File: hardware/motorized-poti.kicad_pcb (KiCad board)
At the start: 2 copper layers, 100 x 20 mm, 31 parts, among them J1 AKL_5_2, P1 CON-SENSOR2, P2 MOTORIZED_POTI, P3 BOOT, P4 CONN_02X04, P5 CONN_02X04, U1 XMC1XXX24, U2 ZXBM5210, U3 DRILL, U4 DRILL, U5 DRILL, U6 DRILL

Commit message: Fix logos
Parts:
- G***: moved to B.Cu
- moved G*** 70.5 mm to (99.3, 100.6)
- moved VAL 1.10 mm to (107.5, 100.6)
- moved G*** 0.90 mm to (115.5, 100.6)

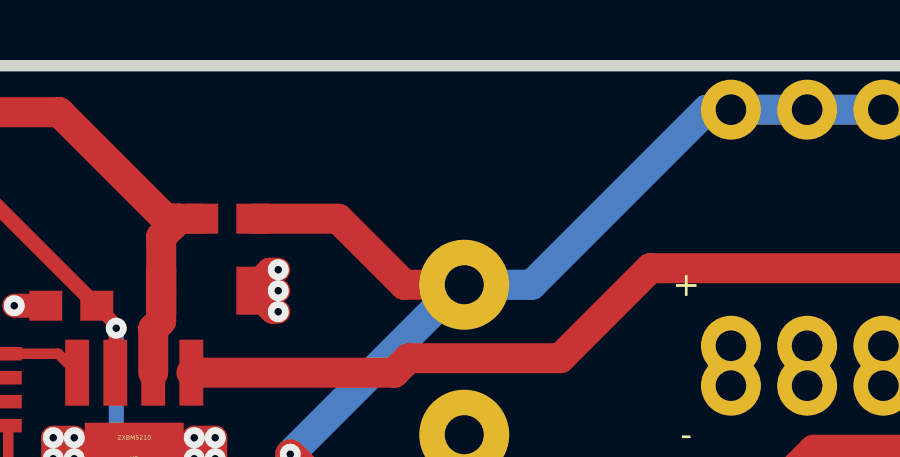
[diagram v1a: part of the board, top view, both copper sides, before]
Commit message: connector distance to short hintt
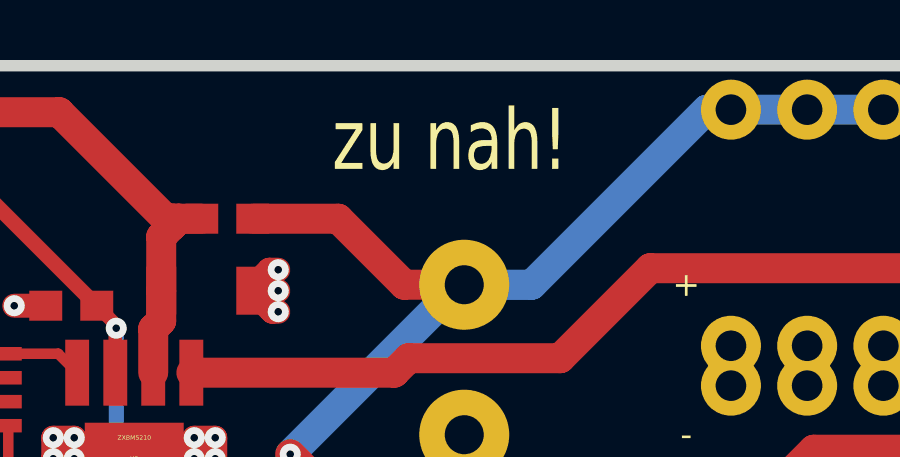
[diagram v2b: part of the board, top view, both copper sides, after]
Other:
- board text added: "zu nah!"
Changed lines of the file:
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@@
-(kicad_pcb (version 4) (host pcbnew 4.0.2+dfsg1-stable)
+(kicad_pcb (version 4) (host pcbnew 4.0.6-e0-6349~53~ubuntu16.04.1)
   (general
     (links 70)
     (no_connects 0)
-    (area 77.409499 90.459499 177.790501 110.840501)
+    (area 70.875139 90.459499 282.795857 162.890793)
     (thickness 1.6002)
-    (drawings 13)
+    (drawings 14)
     (tracks 235)
     (zones 0)
@@
       (net 5 "Net-(P2-PadB)"))
   )
+  (gr_text "zu nah!" (at 141.425 93.15) (layer F.SilkS)
+    (effects (font (size 2.032 1.524) (thickness 0.3048)))
+  )
   (gr_line (start 77.6 93.15) (end 77.6 108.15) (angle 90) (layer Edge.Cuts) (width 0.381))

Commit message: specify part values
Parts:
- C3: value TBD -> 47uF/10V
- L1: value INDUCT -> DNP
- L2: value INDUCT -> FB
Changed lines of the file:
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@@
     (links 70)
     (no_connects 0)
-    (area 70.875139 90.459499 282.795857 162.890793)
+    (area 77.409499 90.459499 177.790501 110.840501)
     (thickness 1.6002)
     (drawings 14)
@@
       (effects (font (size 0.3 0.3) (thickness 0.075)))
     )
-    (fp_text value TBD (at 0 -0.65 180) (layer F.Fab)
+    (fp_text value 47uF/10V (at 0 -0.65 180) (layer F.Fab)
       (effects (font (size 0.3 0.3) (thickness 0.075)))
     )
@@
       (effects (font (size 0.2 0.2) (thickness 0.05)))
     )
-    (fp_text value INDUCT (at 0.05 -0.375 90) (layer F.Fab)
+    (fp_text value DNP (at 0.05 -0.375 90) (layer F.Fab)
       (effects (font (size 0.2 0.2) (thickness 0.05)))
     )
@@
       (effects (font (size 0.2 0.2) (thickness 0.05)))
     )
-    (fp_text value INDUCT (at 0.05 -0.375 180) (layer F.Fab)
+    (fp_text value FB (at 0.05 -0.375 180) (layer F.Fab)
       (effects (font (size 0.2 0.2) (thickness 0.05)))
     )

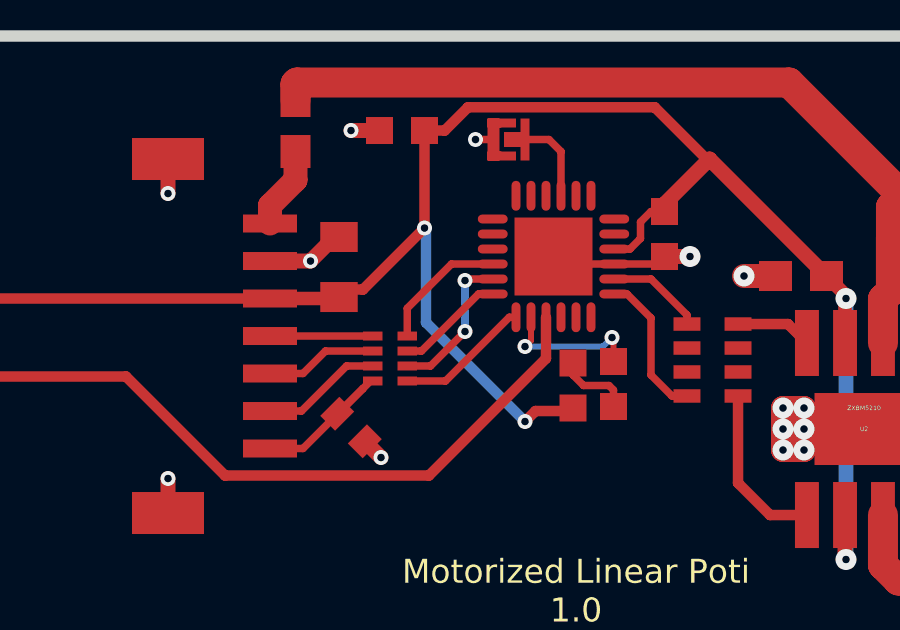
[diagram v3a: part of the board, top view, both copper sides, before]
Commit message: Fix SPI pins
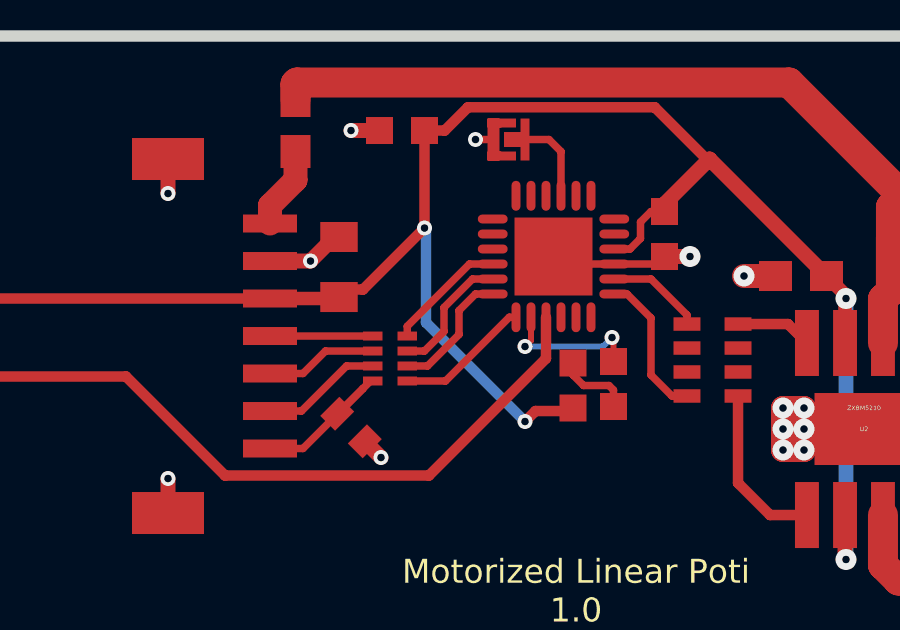
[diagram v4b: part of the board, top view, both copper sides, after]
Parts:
- C2: footprint kicad-libraries:C0805 -> C0805
- C4, C5: footprint kicad-libraries:C0603F -> C0603F
- C6: footprint kicad-libraries:C0402E -> C0402E
- D1: footprint kicad-libraries:D0603F -> D0603F
- J1: footprint kicad-libraries:AKL_5_2 -> AKL_5_2
- L1, L2: footprint kicad-libraries:C0603E -> C0603E
- P1: footprint kicad-libraries:CON-SENSOR2 -> CON-SENSOR2
- P2: footprint kicad-libraries:MOTORIZED_POTI -> MOTORIZED_POTI
- R1: footprint kicad-libraries:R0603F -> R0603F
- RP1: footprint kicad-libraries:4X0603 -> 4X0603
- RP3: footprint kicad-libraries:4X0402 -> 4X0402
- U2: footprint kicad-libraries:SO-8-EP -> SO-8-EP
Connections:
- P2 pad 2: (no net) -> Net-(P2-Pad2)
- RP1 pad 2: (no net) -> Net-(RP1-Pad2)
- RP1 pad 3: (no net) -> Net-(RP1-Pad3)
- RP1 pad 6: (no net) -> Net-(RP1-Pad6)
- RP1 pad 7: (no net) -> Net-(RP1-Pad7)
- U1 pad 11: (no net) -> Net-(U1-Pad11)
- U1 pad 12: (no net) -> Net-(U1-Pad12)
- U1 pad 13: (no net) -> Net-(U1-Pad13)
- U1 pad 14: (no net) -> Net-(U1-Pad14)
- U1 pad 16: (no net) -> Net-(U1-Pad16)
- U1 pad 17: (no net) -> Net-(U1-Pad17)
- U1 pad 18: (no net) -> Net-(U1-Pad18)
- U1 pad 19: (no net) -> Net-(U1-Pad19)
- U1 pad 20: (no net) -> Net-(U1-Pad20)
- U1 pad 21: (no net) -> Net-(U1-Pad21)
- U1 pad 23: S-MOSI -> S-CLK
- U1 pad 24: S-CLK -> S-MOSI
- U1 pad 4: (no net) -> Net-(U1-Pad4)
- U1 pad 5: (no net) -> Net-(U1-Pad5)
- U1 pad 6: (no net) -> Net-(U1-Pad6)
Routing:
- net S-MOSI: track 5.05 -> 4.31 mm, vias 2 -> 0
- net S-CLK: track 3.64 -> 4.31 mm

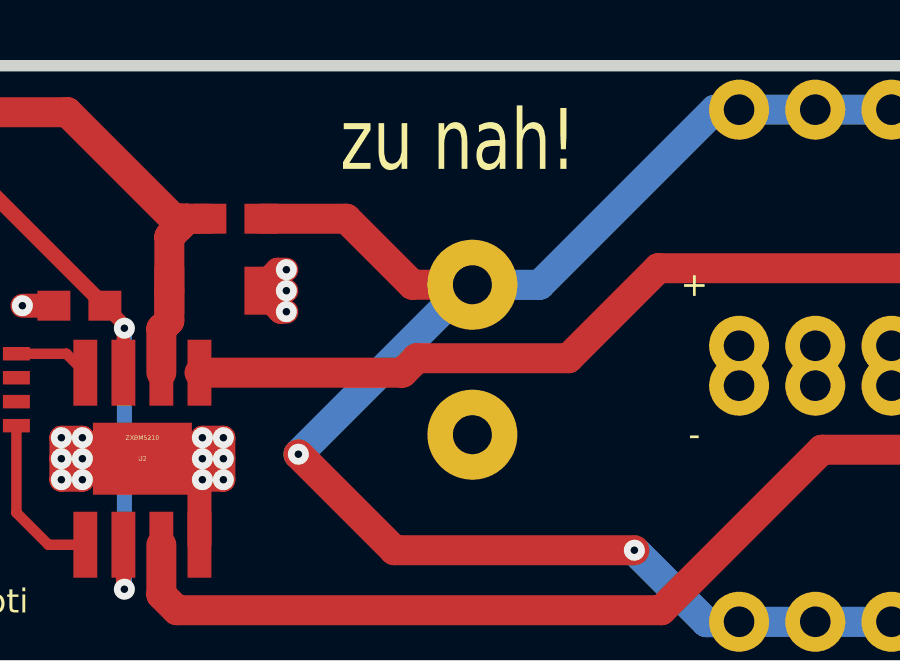
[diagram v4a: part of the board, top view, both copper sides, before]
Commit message: Fix orientation of J1
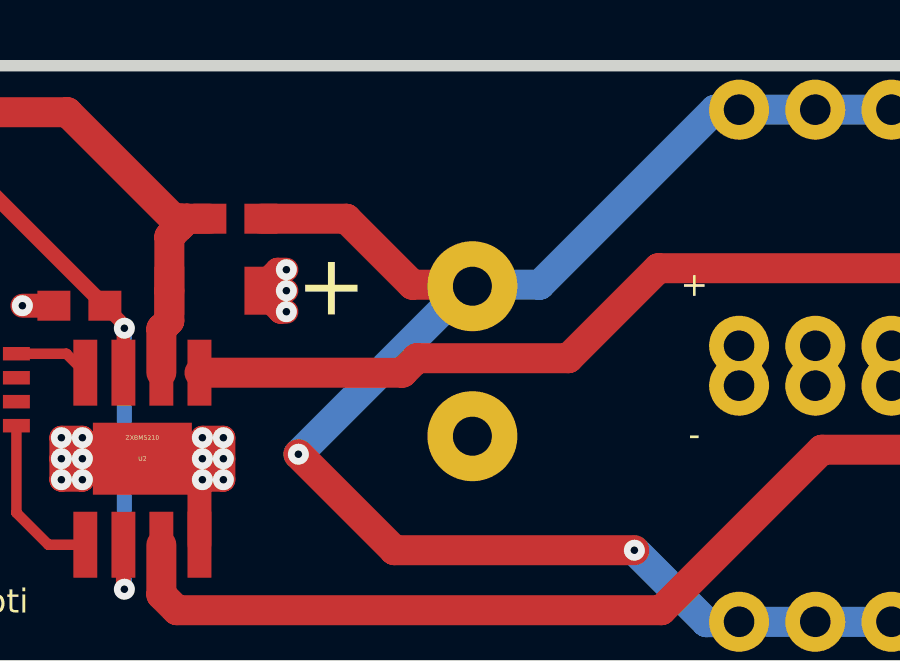
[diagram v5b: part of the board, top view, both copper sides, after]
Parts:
- turned J1 to 90 degrees
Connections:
- J1 pad 1: PWR -> GND
- J1 pad 2: GND -> PWR
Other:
- board text removed: "zu nah!"
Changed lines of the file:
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@@
     (links 70)
     (no_connects 0)
-    (area 77.409499 90.459499 177.790501 110.840501)
+    (area 70.875139 90.459499 282.895869 162.490743)
     (thickness 1.6002)
     (drawings 14)
@@
   (title_block
     (title "Motorized Linear Poti Bricklet")
-    (date 2017-05-05)
+    (date 2017-05-19)
     (rev 1.0)
     (company "Tinkerforge GmbH")
@@
     (35 F.Paste user)
     (36 B.SilkS user hide)
-    (37 F.SilkS user hide)
+    (37 F.SilkS user)
     (38 B.Mask user)
     (39 F.Mask user)
@@
   )
   (setup
-    (last_trace_width 0.25)
+    (last_trace_width 0.249)
     (user_trace_width 0.2)
     (user_trace_width 0.25)
@@
   )
   (module AKL_5_2 (layer Vorderseite)
-    (at 141.9 100.45 270)
-    (fp_text reference J1 (at 0 2.60096 270) (layer F.Fab)
+    (at 141.9 100.5 90)
+    (fp_text reference J1 (at 0 2.60096 90) (layer F.Fab)
       (effects (font (size 0.59944 0.59944) (thickness 0.12446)))
     )
-    (fp_text value AKL_5_2 (at -0.0508 -2.55016 270) (layer F.Fab)
+    (fp_text value AKL_5_2 (at -0.0508 -2.55016 90) (layer F.Fab)
       (effects (font (size 0.29972 0.29972) (thickness 0.07493)))
     )
@@
     (fp_line (start 5.00126 -3.59918) (end -5.00126 -3.59918) (layer F.Fab) (width 0.15))
     (fp_line (start -5.00126 -3.60172) (end -5.00126 4.0005) (layer F.Fab) (width 0.15))
-    (pad 1 thru_hole circle (at -2.49936 0 270) (size 2.99974 2.99974) (drill 1.30048) (layers *.Cu *.Mask F.SilkS)
-      (net 19 PWR))
-    (pad 2 thru_hole circle (at 2.49936 0 270) (size 2.99974 2.99974) (drill 1.30048) (layers *.Cu *.Mask F.SilkS)
+    (pad 1 thru_hole circle (at -2.49936 0 90) (size 2.99974 2.99974) (drill 1.30048) (layers *.Cu *.Mask F.SilkS)
       (net 1 GND))
+    (pad 2 thru_hole circle (at 2.49936 0 90) (size 2.99974 2.99974) (drill 1.30048) (layers *.Cu *.Mask F.SilkS)
+      (net 19 PWR))
     (model Connectors/AKL_5_2.wrl
       (at (xyz 0 -0.02 0))
@@
       (net 1 GND))
   )
-  (gr_text "zu nah!" (at 141.425 93.15) (layer F.SilkS)
-    (effects (font (size 2.032 1.524) (thickness 0.3048)))
+  (gr_text + (at 137.2 98) (layer F.SilkS)
+    (effects (font (size 2.032 2.032) (thickness 0.3048)))
   )
   (gr_line (start 77.6 93.15) (end 77.6 108.15) (angle 90) (layer Edge.Cuts) (width 0.381))
@@
   (segment (start 119.075 100.025) (end 119.3 100.025) (width 0.25) (layer Vorderseite) (net 10))
   (segment (start 116.9507 102.1493) (end 119.075 100.025) (width 0.25) (layer Vorderseite) (net 10))
-  (segment (start 115.675 101.64892) (end 116.35108 101.64892) (width 0.25) (layer Vorderseite) (net 11) (status 400000))
-  (segment (start 117.95 99.25) (end 118.525 99.25) (width 0.25) (layer Vorderseite) (net 11) (status 800000))
+  (segment (start 115.675 101.64892) (end 116.35108 101.64892) (width 0.25) (layer Vorderseite) (net 11))
+  (segment (start 117.95 99.25) (end 118.525 99.25) (width 0.25) (layer Vorderseite) (net 11))
   (segment (start 117.4 99.8) (end 117.95 99.25) (width 0.25) (layer Vorderseite) (net 11))
   (segment (start 117.4 100.6) (end 117.4 99.8) (width 0.25) (layer Vorderseite) (net 11))
   (segment (start 116.35108 101.64892) (end 117.4 100.6) (width 0.25) (layer Vorderseite) (net 11))
-  (segment (start 115.675 101.15108) (end 116.24892 101.15108) (width 0.25) (layer Vorderseite) (net 12) (status 400000))
-  (segment (start 117.85 98.75) (end 118.525 98.75) (width 0.25) (layer Vorderseite) (net 12) (status 800000))
+  (segment (start 115.675 101.15108) (end 116.24892 101.15108) (width 0.25) (layer Vorderseite) (net 12))
+  (segment (start 117.85 98.75) (end 118.525 98.75) (width 0.25) (layer Vorderseite) (net 12))
   (segment (start 116.9 99.7) (end 117.85 98.75) (width 0.25) (layer Vorderseite) (net 12))
   (segment (start 116.9 100.5) (end 116.9 99.7) (width 0.25) (layer Vorderseite) (net 12))
   (segment (start 116.24892 101.15108) (end 116.9 100.5) (width 0.25) (layer Vorderseite) (net 12))
-  (segment (start 115.675 100.6507) (end 115.675 100.325) (width 0.25) (layer Vorderseite) (net 13) (status 400000))
-  (segment (start 117.75 98.25) (end 118.525 98.25) (width 0.25) (layer Vorderseite) (net 13) (status 800000))
+  (segment (start 115.675 100.6507) (end 115.675 100.325) (width 0.25) (layer Vorderseite) (net 13))
+  (segment (start 117.75 98.25) (end 118.525 98.25) (width 0.25) (layer Vorderseite) (net 13))
   (segment (start 115.675 100.325) (end 117.75 98.25) (width 0.25) (layer Vorderseite) (net 13))
   (segment (start 119.2 94.1) (end 119.6 94.1) (width 0.2) (layer Vorderseite) (net 14))
@@
   (segment (start 122.55 102.45) (end 122.4 102.3) (width 0.25) (layer Vorderseite) (net 18))
   (segment (start 121.2 101.95) (end 121.2 101.4499) (width 0.25) (layer Vorderseite) (net 18))
+  (segment (start 136.1 103.6) (end 141.74936 97.95064) (width 1.00076) (layer Rückseite) (net 19))
+  (segment (start 141.74936 97.95064) (end 144.14936 97.95064) (width 1.00076) (layer Rückseite) (net 19))
+  (segment (start 139.90064 97.95064) (end 141.9 97.95064) (width 1.00076) (layer Vorderseite) (net 19))
   (segment (start 158.41 109.185) (end 155.87 109.185) (width 1.00076) (layer Rückseite) (net 19))
   (segment (start 155.87 109.185) (end 153.33 109.185) (width 1.00076) (layer Rückseite) (net 19))
@@
   (segment (start 136.1 103.6) (end 136.1 103.6) (width 1.00076) (layer Vorderseite) (net 19))
   (via (at 136.1 103.6) (size 0.70104) (drill 0.24892) (layers Vorderseite Rückseite) (net 19))
-  (segment (start 136.1 103.6) (end 141.74936 97.95064) (width 1.00076) (layer Rückseite) (net 19))
-  (segment (start 141.74936 97.95064) (end 144.14936 97.95064) (width 1.00076) (layer Rückseite) (net 19))
   (segment (start 144.14936 97.95064) (end 149.985 92.115) (width 1.00076) (layer Rückseite) (net 19))
   (segment (start 149.985 92.115) (end 153.33 92.115) (width 1.00076) (layer Rückseite) (net 19))
@@
   (segment (start 155.87 92.115) (end 158.41 92.115) (width 1.00076) (layer Rückseite) (net 19))
   (segment (start 134.8501 95.75) (end 137.7 95.75) (width 1.00076) (layer Vorderseite) (net 19))
-  (segment (start 139.90064 97.95064) (end 141.9 97.95064) (width 1.00076) (layer Vorderseite) (net 19))
   (segment (start 137.7 95.75) (end 139.90064 97.95064) (width 1.00076) (layer Vorderseite) (net 19))
   (segment (start 113.340381 103.240381) (end 113.359619 103.240381) (width 0.25) (layer Vorderseite) (net 20))

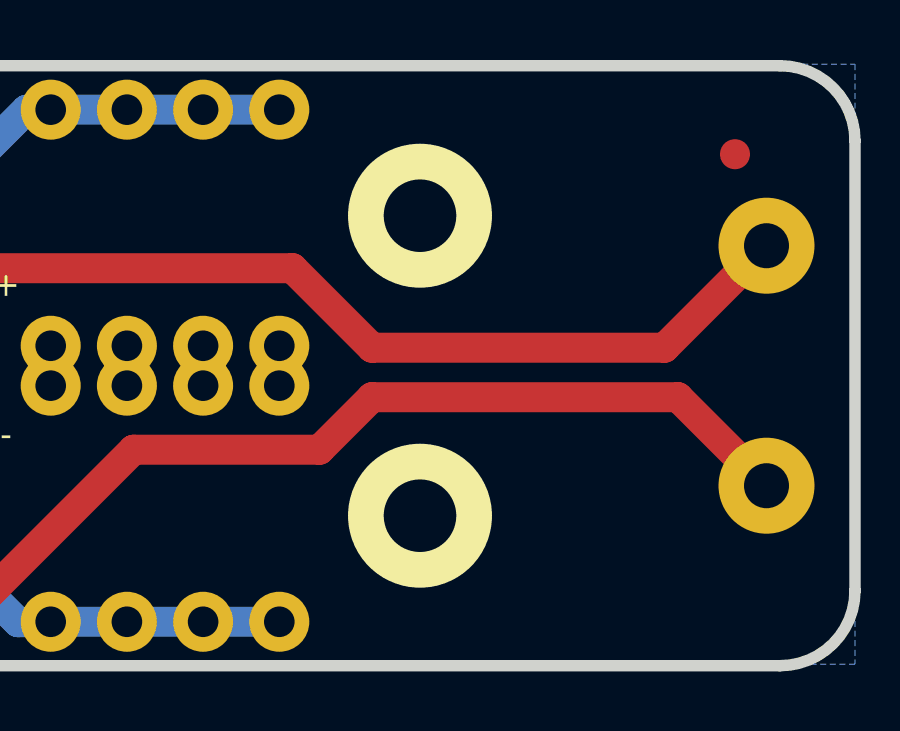
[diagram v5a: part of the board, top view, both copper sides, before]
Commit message: Fix drill holes to grid
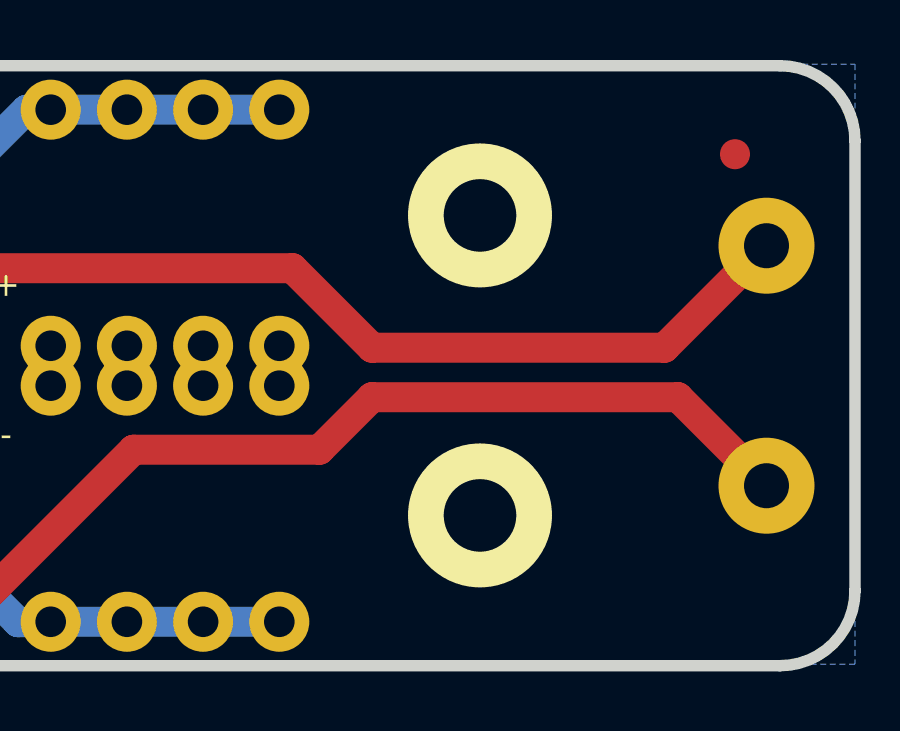
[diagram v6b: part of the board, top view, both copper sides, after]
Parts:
- moved U5 2.00 mm to (165.1, 95.6)
- moved U6 2.00 mm to (165.1, 105.6)
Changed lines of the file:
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@@
     (links 70)
     (no_connects 0)
-    (area 70.875139 90.459499 282.895869 162.490743)
+    (area 77.409499 90.459499 177.790501 110.840501)
     (thickness 1.6002)
     (drawings 14)
@@
     (34 B.Paste user)
     (35 F.Paste user)
-    (36 B.SilkS user hide)
+    (36 B.SilkS user)
     (37 F.SilkS user)
     (38 B.Mask user)
@@
   )
   (module kicad-libraries:DRILL_NP (layer Vorderseite)
-    (at 163.1 105.65 90)
+    (at 165.1 105.64 90)
     (fp_text reference U6 (at 0 0 90) (layer F.SilkS) hide
       (effects (font (size 0.29972 0.29972) (thickness 0.0762)))
@@
   )
   (module kicad-libraries:DRILL_NP (layer Vorderseite)
-    (at 163.1 95.65)
+    (at 165.1 95.64)
     (fp_text reference U5 (at 0 0) (layer F.SilkS) hide
       (effects (font (size 0.29972 0.29972) (thickness 0.0762)))

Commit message: Add 3d: motor driver
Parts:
- U2: footprint SO-8-EP -> kicad-libraries:SO-8-EP
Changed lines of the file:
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@@
       (net 13 S-CS))
   )
-  (module SO-8-EP (layer Vorderseite)
+  (module kicad-libraries:SO-8-EP (layer Vorderseite)
     (at 130.9 103.75 180)
     (fp_text reference U2 (at 0 0 180) (layer F.SilkS)
@@
     (pad EP smd rect (at 0 0 180) (size 3.3 2.4) (layers Vorderseite F.Paste F.Mask)
       (net 1 GND))
+    (model Housing_SO/SO-8.wrl
+      (at (xyz 0 0 0))
+      (scale (xyz 1 1 1))
+      (rotate (xyz 90 180 180))
+    )
   )
   (gr_text + (at 137.2 98) (layer F.SilkS)
